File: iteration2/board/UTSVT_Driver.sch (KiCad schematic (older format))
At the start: 4 parts, among them J1 DB37_Female_MountingHoles, U1 Nucleo, U2 SN65HVD230

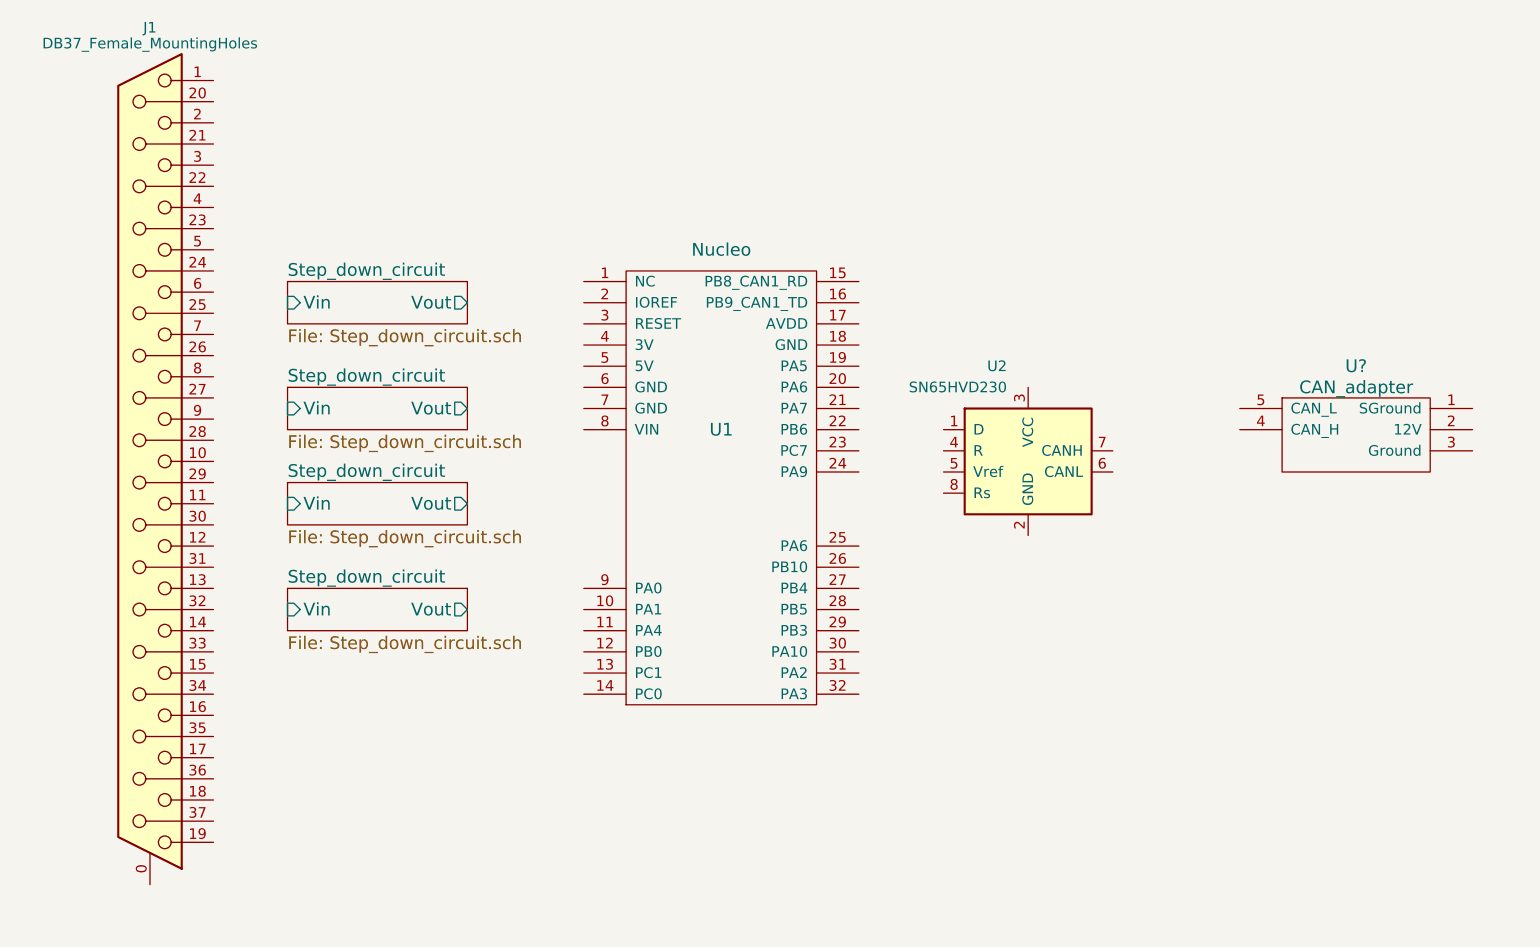
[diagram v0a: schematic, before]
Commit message: Added traces
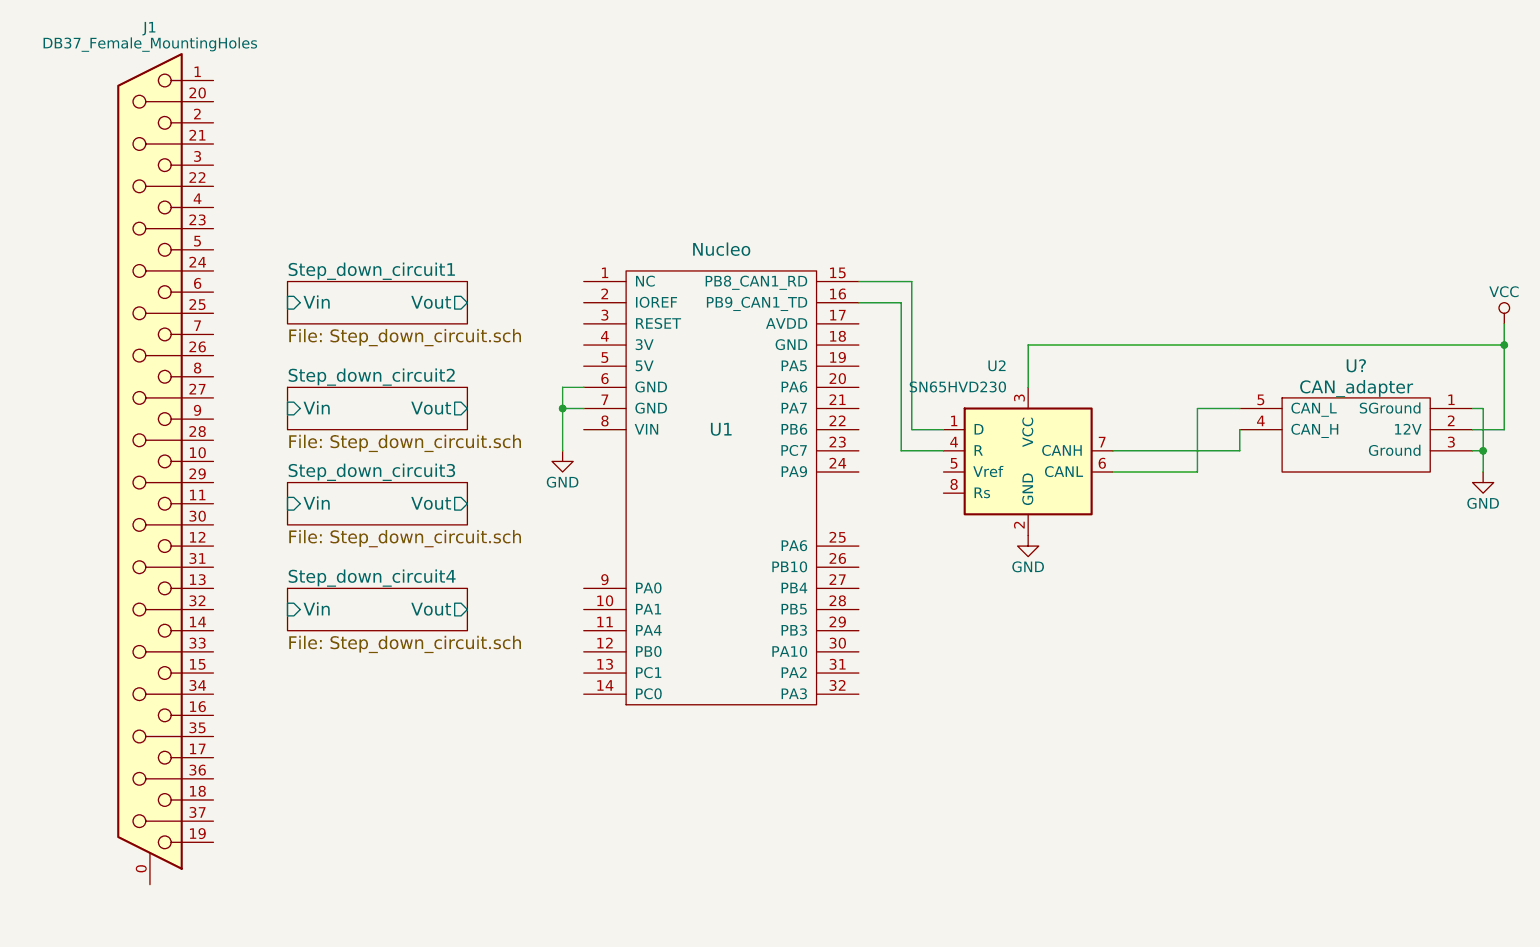
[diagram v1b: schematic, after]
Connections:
- net at U1.15 (PB8_CAN1_RD): now also U2.1 (D)
- net at U1.16 (PB9_CAN1_TD): now also U2.4 (R)
- net GND: now reaches U1.6 (GND)
- net GND: now also U1.7 (GND), U2.2 (GND), U?.1 (SGround), U?.3 (Ground)
- net VCC: now reaches U2.3 (VCC)
- net VCC: now also U?.2 (12V)
- net at U2.6 (CANL): now also U?.5 (CAN_L)
- net at U2.7 (CANH): now also U?.4 (CAN_H)
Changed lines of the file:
@@
 S 4050 3050 850  200
 U 59EC784F
-F0 "Step_down_circuit" 60
+F0 "Step_down_circuit1" 60
 F1 "Step_down_circuit.sch" 60
 F2 "Vin" I L 4050 3150 60
@@
 S 4050 3550 850  200
 U 59EC8586
-F0 "Step_down_circuit" 60
+F0 "Step_down_circuit2" 60
 F1 "Step_down_circuit.sch" 60
 F2 "Vin" I L 4050 3650 60
@@
 S 4050 4000 850  200
 U 59EC8F0E
-F0 "Step_down_circuit" 60
+F0 "Step_down_circuit3" 60
 F1 "Step_down_circuit.sch" 60
 F2 "Vin" I L 4050 4100 60
@@
 S 4050 4500 850  200
 U 59EC8F12
-F0 "Step_down_circuit" 60
+F0 "Step_down_circuit4" 60
 F1 "Step_down_circuit.sch" 60
 F2 "Vin" I L 4050 4600 60
@@
 	1    0    0    -1
 $EndComp
+$Comp
+L GND #PWR?
+U 1 1 59F244D9
+P 9700 3950
+F 0 "#PWR?" H 9700 3700 50  0001 C CNN
+F 1 "GND" H 9700 3800 50  0000 C CNN
+F 2 "" H 9700 3950 50  0001 C CNN
+F 3 "" H 9700 3950 50  0001 C CNN
+	1    9700 3950
+	1    0    0    -1
+$EndComp
+$Comp
+L GND #PWR?
+U 1 1 59F24541
+P 7550 4250
+F 0 "#PWR?" H 7550 4000 50  0001 C CNN
+F 1 "GND" H 7550 4100 50  0000 C CNN
+F 2 "" H 7550 4250 50  0001 C CNN
+F 3 "" H 7550 4250 50  0001 C CNN
+	1    7550 4250
+	1    0    0    -1
+$EndComp
+$Comp
+L GND #PWR?
+U 1 1 59F262C8
+P 5350 3850
+F 0 "#PWR?" H 5350 3600 50  0001 C CNN
+F 1 "GND" H 5350 3700 50  0000 C CNN
+F 2 "" H 5350 3850 50  0001 C CNN
+F 3 "" H 5350 3850 50  0001 C CNN
+	1    5350 3850
+	1    0    0    -1
+$EndComp
+$Comp
+L VCC #PWR?
+U 1 1 59F2677A
+P 9800 3250
+F 0 "#PWR?" H 9800 3100 50  0001 C CNN
+F 1 "VCC" H 9800 3400 50  0000 C CNN
+F 2 "" H 9800 3250 50  0001 C CNN
+F 3 "" H 9800 3250 50  0001 C CNN
+	1    9800 3250
+	1    0    0    -1
+$EndComp
+Wire Wire Line
+	7950 3850 8550 3850
+Wire Wire Line
+	8550 3850 8550 3750
+Wire Wire Line
+	7950 3950 8350 3950
+Wire Wire Line
+	8350 3950 8350 3650
+Wire Wire Line
+	8350 3650 8550 3650
+Wire Wire Line
+	5450 3550 5350 3550
+Wire Wire Line
+	5350 3550 5350 3850
+Wire Wire Line
+	5450 3650 5350 3650
+Connection ~ 5350 3650
+Wire Wire Line
+	6750 3050 7000 3050
+Wire Wire Line
+	7000 3050 7000 3750
+Wire Wire Line
+	7000 3750 7150 3750
+Wire Wire Line
+	6750 3150 6950 3150
+Wire Wire Line
+	6950 3150 6950 3850
+Wire Wire Line
+	6950 3850 7150 3850
+Wire Wire Line
+	9800 3250 9800 3750
+Wire Wire Line
+	9800 3750 9650 3750
+Wire Wire Line
+	9650 3650 9700 3650
+Wire Wire Line
+	9700 3650 9700 3950
+Wire Wire Line
+	9700 3850 9650 3850
+Connection ~ 9700 3850
+Wire Wire Line
+	7550 3550 7550 3350
+Wire Wire Line
+	7550 3350 9800 3350
+Connection ~ 9800 3350
 $EndSCHEMATC

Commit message: Modified to accept potentiometer input
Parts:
- added C?: C, symbol C
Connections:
- net GND: now also C?.1
- net VCC: no longer U2.3 (VCC)
- net step_down_circuit2/Vout: now reaches U1.10 (PA1)
- net step_down_circuit3/Vout: now reaches U1.11 (PA4)
- net step_down_circuit_analog1/Vout: now reaches U1.12 (PB0)
- net step_down_circuit1/Vout: now reaches U1.9 (PA0)
- new net +3V3: C?.2, U2.3 (VCC)
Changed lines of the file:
@@
 S 4050 3050 850  200
 U 59EC784F
-F0 "Step_down_circuit1" 60
-F1 "Step_down_circuit.sch" 60
+F0 "step_down_circuit1" 60
+F1 "step_down_circuit.sch" 60
 F2 "Vin" I L 4050 3150 60
 F3 "Vout" O R 4900 3150 60
@@
 S 4050 3550 850  200
 U 59EC8586
-F0 "Step_down_circuit2" 60
-F1 "Step_down_circuit.sch" 60
+F0 "step_down_circuit2" 60
+F1 "step_down_circuit.sch" 60
 F2 "Vin" I L 4050 3650 60
 F3 "Vout" O R 4900 3650 60
@@
 S 4050 4000 850  200
 U 59EC8F0E
-F0 "Step_down_circuit3" 60
-F1 "Step_down_circuit.sch" 60
+F0 "step_down_circuit3" 60
+F1 "step_down_circuit.sch" 60
 F2 "Vin" I L 4050 4100 60
 F3 "Vout" O R 4900 4100 60
-$EndSheet
-$Sheet
-S 4050 4500 850  200
-U 59EC8F12
-F0 "Step_down_circuit4" 60
-F1 "Step_down_circuit.sch" 60
-F2 "Vin" I L 4050 4600 60
-F3 "Vout" O R 4900 4600 60
 $EndSheet
 $Comp
@@
 	1    0    0    -1
 $EndComp
+$Sheet
+S 4050 4450 850  200
+U 59F275D4
+F0 "step_down_circuit_analog1" 60
+F1 "step_down_circuit_analog.sch" 60
+F2 "Vin" I L 4050 4550 60
+F3 "Vout" O R 4900 4550 60
+$EndSheet
+$Comp
+L GND #PWR?
+U 1 1 59F29663
+P 7850 3350
+F 0 "#PWR?" H 7850 3100 50  0001 C CNN
+F 1 "GND" H 7850 3200 50  0000 C CNN
+F 2 "" H 7850 3350 50  0001 C CNN
+F 3 "" H 7850 3350 50  0001 C CNN
+	1    7850 3350
+	1    0    0    -1
+$EndComp
+$Comp
+L +3.3V #PWR?
+U 1 1 59F296AF
+P 7550 3250
+F 0 "#PWR?" H 7550 3100 50  0001 C CNN
+F 1 "+3.3V" H 7550 3390 50  0000 C CNN
+F 2 "" H 7550 3250 50  0001 C CNN
+F 3 "" H 7550 3250 50  0001 C CNN
+	1    7550 3250
+	1    0    0    -1
+$EndComp
+$Comp
+L C C?
+U 1 1 59F29741
+P 7700 3350
+F 0 "C?" H 7725 3450 50  0000 L CNN
+F 1 "C" H 7725 3250 50  0000 L CNN
+F 2 "" H 7738 3200 50  0001 C CNN
+F 3 "" H 7700 3350 50  0001 C CNN
+	1    7700 3350
+	0    1    1    0
+$EndComp
 Wire Wire Line
 	7950 3850 8550 3850
@@
 	9700 3850 9650 3850
 Connection ~ 9700 3850
+Connection ~ 9800 3350
 Wire Wire Line
-	7550 3550 7550 3350
+	7550 3250 7550 3550
+Connection ~ 7550 3350
 Wire Wire Line
-	7550 3350 9800 3350
-Connection ~ 9800 3350
+	4900 3150 5050 3150
+Wire Wire Line
+	5050 3150 5050 4500
+Wire Wire Line
+	5050 4500 5450 4500
+Wire Wire Line
+	4900 3650 5100 3650
+Wire Wire Line
+	5100 3650 5100 4600
+Wire Wire Line
+	5100 4600 5450 4600
+Wire Wire Line
+	4900 4100 5150 4100
+Wire Wire Line
+	5150 4100 5150 4700
+Wire Wire Line
+	5150 4700 5450 4700
+Wire Wire Line
+	4900 4550 5200 4550
+Wire Wire Line
+	5200 4550 5200 4800
+Wire Wire Line
+	5200 4800 5450 4800
 $EndSCHEMATC

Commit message: Update Netlist
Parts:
- C1: renamed from C?; footprint (none) -> Capacitors_SMD:C_0805_HandSoldering
- U1: footprint (none) -> MotorControllerStuff:AFBShieldBoard
- U3: renamed from U?; footprint (none) -> MotorControllerStuff:CANadapter
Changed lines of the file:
@@
 F 0 "U1" H 6100 4350 60  0000 C CNN
 F 1 "Nucleo" H 6100 5200 60  0000 C CNN
-F 2 "" H 6100 4350 60  0001 C CNN
+F 2 "MotorControllerStuff:AFBShieldBoard" H 6100 4350 60  0001 C CNN
 F 3 "" H 6100 4350 60  0001 C CNN
 	1    6100 4050
@@
 $EndSheet
 $Comp
-L CAN_adapter U?
+L CAN_adapter U3
 U 1 1 59EC9235
 P 9100 3750
-F 0 "U?" H 9100 4050 60  0000 C CNN
+F 0 "U3" H 9100 4050 60  0000 C CNN
 F 1 "CAN_adapter" H 9100 3950 60  0000 C CNN
-F 2 "" H 9150 3750 60  0001 C CNN
+F 2 "MotorControllerStuff:CANadapter" H 9150 3750 60  0001 C CNN
 F 3 "" H 9150 3750 60  0001 C CNN
 	1    9100 3750
@@
 $EndComp
 $Comp
-L GND #PWR?
+L GND #PWR5
 U 1 1 59F244D9
 P 9700 3950
-F 0 "#PWR?" H 9700 3700 50  0001 C CNN
+F 0 "#PWR5" H 9700 3700 50  0001 C CNN
 F 1 "GND" H 9700 3800 50  0000 C CNN
 F 2 "" H 9700 3950 50  0001 C CNN
@@
 $EndComp
 $Comp
-L GND #PWR?
+L GND #PWR3
 U 1 1 59F24541
 P 7550 4250
-F 0 "#PWR?" H 7550 4000 50  0001 C CNN
+F 0 "#PWR3" H 7550 4000 50  0001 C CNN
 F 1 "GND" H 7550 4100 50  0000 C CNN
 F 2 "" H 7550 4250 50  0001 C CNN
@@
 $EndComp
 $Comp
-L GND #PWR?
+L GND #PWR1
 U 1 1 59F262C8
 P 5350 3850
-F 0 "#PWR?" H 5350 3600 50  0001 C CNN
+F 0 "#PWR1" H 5350 3600 50  0001 C CNN
 F 1 "GND" H 5350 3700 50  0000 C CNN
 F 2 "" H 5350 3850 50  0001 C CNN
@@
 $EndComp
 $Comp
-L VCC #PWR?
+L VCC #PWR6
 U 1 1 59F2677A
 P 9800 3250
-F 0 "#PWR?" H 9800 3100 50  0001 C CNN
+F 0 "#PWR6" H 9800 3100 50  0001 C CNN
 F 1 "VCC" H 9800 3400 50  0000 C CNN
 F 2 "" H 9800 3250 50  0001 C CNN
@@
 $EndSheet
 $Comp
-L GND #PWR?
+L GND #PWR4
 U 1 1 59F29663
 P 7850 3350
-F 0 "#PWR?" H 7850 3100 50  0001 C CNN
+F 0 "#PWR4" H 7850 3100 50  0001 C CNN
 F 1 "GND" H 7850 3200 50  0000 C CNN
 F 2 "" H 7850 3350 50  0001 C CNN
@@
 $EndComp
 $Comp
-L +3.3V #PWR?
+L +3.3V #PWR2
 U 1 1 59F296AF
 P 7550 3250
-F 0 "#PWR?" H 7550 3100 50  0001 C CNN
+F 0 "#PWR2" H 7550 3100 50  0001 C CNN
 F 1 "+3.3V" H 7550 3390 50  0000 C CNN
 F 2 "" H 7550 3250 50  0001 C CNN
@@
 $EndComp
 $Comp
-L C C?
+L C C1
 U 1 1 59F29741
 P 7700 3350
-F 0 "C?" H 7725 3450 50  0000 L CNN
+F 0 "C1" H 7725 3450 50  0000 L CNN
 F 1 "C" H 7725 3250 50  0000 L CNN
-F 2 "" H 7738 3200 50  0001 C CNN
+F 2 "Capacitors_SMD:C_0805_HandSoldering" H 7738 3200 50  0001 C CNN
 F 3 "" H 7700 3350 50  0001 C CNN
 	1    7700 3350

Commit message: Redo netlist
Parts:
- J1: footprint (none) -> Connectors_DSub:DB37FC
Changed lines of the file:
@@
 F 0 "J1" H 3400 5950 50  0000 C CNN
 F 1 "DB37_Female_MountingHoles" H 3400 5875 50  0000 C CNN
-F 2 "" H 3400 3900 50  0001 C CNN
+F 2 "Connectors_DSub:DB37FC" H 3400 3900 50  0001 C CNN
 F 3 "" H 3400 3900 50  0001 C CNN
 	1    3400 3900

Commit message: finish wiring
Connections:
- net step_down_circuit1/Vin: now also J1.10
- net step_down_circuit2/Vin: now also J1.12
- net step_down_circuit3/Vin: now also J1.14
- net step_down_circuit_analog1/Vin: now also J1.3
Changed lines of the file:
@@
 $EndComp
 $Comp
-L GND #PWR5
+L GND #PWR01
 U 1 1 59F244D9
 P 9700 3950
-F 0 "#PWR5" H 9700 3700 50  0001 C CNN
+F 0 "#PWR01" H 9700 3700 50  0001 C CNN
 F 1 "GND" H 9700 3800 50  0000 C CNN
 F 2 "" H 9700 3950 50  0001 C CNN
@@
 $EndComp
 $Comp
-L GND #PWR3
+L GND #PWR02
 U 1 1 59F24541
 P 7550 4250
-F 0 "#PWR3" H 7550 4000 50  0001 C CNN
+F 0 "#PWR02" H 7550 4000 50  0001 C CNN
 F 1 "GND" H 7550 4100 50  0000 C CNN
 F 2 "" H 7550 4250 50  0001 C CNN
@@
 $EndComp
 $Comp
-L GND #PWR1
+L GND #PWR03
 U 1 1 59F262C8
 P 5350 3850
-F 0 "#PWR1" H 5350 3600 50  0001 C CNN
+F 0 "#PWR03" H 5350 3600 50  0001 C CNN
 F 1 "GND" H 5350 3700 50  0000 C CNN
 F 2 "" H 5350 3850 50  0001 C CNN
@@
 $EndComp
 $Comp
-L VCC #PWR6
+L VCC #PWR04
 U 1 1 59F2677A
 P 9800 3250
-F 0 "#PWR6" H 9800 3100 50  0001 C CNN
+F 0 "#PWR04" H 9800 3100 50  0001 C CNN
 F 1 "VCC" H 9800 3400 50  0000 C CNN
 F 2 "" H 9800 3250 50  0001 C CNN
@@
 $EndSheet
 $Comp
-L GND #PWR4
+L GND #PWR05
 U 1 1 59F29663
 P 7850 3350
-F 0 "#PWR4" H 7850 3100 50  0001 C CNN
+F 0 "#PWR05" H 7850 3100 50  0001 C CNN
 F 1 "GND" H 7850 3200 50  0000 C CNN
 F 2 "" H 7850 3350 50  0001 C CNN
@@
 $EndComp
 $Comp
-L +3.3V #PWR2
+L +3.3V #PWR06
 U 1 1 59F296AF
 P 7550 3250
-F 0 "#PWR2" H 7550 3100 50  0001 C CNN
+F 0 "#PWR06" H 7550 3100 50  0001 C CNN
 F 1 "+3.3V" H 7550 3390 50  0000 C CNN
 F 2 "" H 7550 3250 50  0001 C CNN
@@
 	5150 4700 5450 4700
 Wire Wire Line
-	4900 4550 5200 4550
+	3700 2500 4000 2500
+Wire Wire Line
+	4000 2500 4000 4550
+Wire Wire Line
+	4000 4550 4050 4550
+Wire Wire Line
+	3700 4300 3950 4300
+Wire Wire Line
+	3950 4300 3950 3650
+Wire Wire Line
+	3950 3650 4050 3650
+Wire Wire Line
+	3700 3900 3900 3900
+Wire Wire Line
+	3900 3900 3900 3150
+Wire Wire Line
+	3900 3150 4050 3150
+Wire Wire Line
+	3700 4700 3900 4700
+Wire Wire Line
+	3900 4700 3900 4100
+Wire Wire Line
+	3900 4100 4050 4100
 Wire Wire Line
 	5200 4550 5200 4800
 Wire Wire Line
 	5200 4800 5450 4800
+Wire Wire Line
+	4900 4550 5200 4550
 $EndSCHEMATC

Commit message: Generated netlist
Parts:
- U1: footprint MotorControllerStuff:AFBShieldBoard -> UTSVT_board:AFBShieldBoard
- U3: footprint MotorControllerStuff:CANadapter -> UTSVT_board:CAN_adapter
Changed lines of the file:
@@
 F 0 "U1" H 6100 4350 60  0000 C CNN
 F 1 "Nucleo" H 6100 5200 60  0000 C CNN
-F 2 "MotorControllerStuff:AFBShieldBoard" H 6100 4350 60  0001 C CNN
+F 2 "UTSVT_board:AFBShieldBoard" H 6100 4350 60  0001 C CNN
 F 3 "" H 6100 4350 60  0001 C CNN
 	1    6100 4050
@@
 F 0 "U3" H 9100 4050 60  0000 C CNN
 F 1 "CAN_adapter" H 9100 3950 60  0000 C CNN
-F 2 "MotorControllerStuff:CANadapter" H 9150 3750 60  0001 C CNN
+F 2 "UTSVT_board:CAN_adapter" H 9150 3750 60  0001 C CNN
 F 3 "" H 9150 3750 60  0001 C CNN
 	1    9100 3750

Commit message: Redid some components to fit footprint
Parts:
- J1: footprint Connectors_DSub:DB37FC -> UTSVT_board:DB37FC
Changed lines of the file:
@@
 $EndDescr
-$Comp
-L Nucleo U1
-U 1 1 59EB7F2F
-P 6100 4050
-F 0 "U1" H 6100 4350 60  0000 C CNN
-F 1 "Nucleo" H 6100 5200 60  0000 C CNN
-F 2 "UTSVT_board:AFBShieldBoard" H 6100 4350 60  0001 C CNN
-F 3 "" H 6100 4350 60  0001 C CNN
-	1    6100 4050
-	1    0    0    -1
-$EndComp
 $Comp
 L DB37_Female_MountingHoles J1
@@
 F 0 "J1" H 3400 5950 50  0000 C CNN
 F 1 "DB37_Female_MountingHoles" H 3400 5875 50  0000 C CNN
-F 2 "Connectors_DSub:DB37FC" H 3400 3900 50  0001 C CNN
+F 2 "UTSVT_board:DB37FC" H 3400 3900 50  0001 C CNN
 F 3 "" H 3400 3900 50  0001 C CNN
 	1    3400 3900
@@
 Wire Wire Line
 	4900 4550 5200 4550
+$Comp
+L Nucleo U1
+U 1 1 59F29930
+P 6100 4050
+F 0 "U1" H 6100 4350 60  0000 C CNN
+F 1 "Nucleo" H 6100 5200 60  0000 C CNN
+F 2 "UTSVT_board:AFBShieldBoard" H 6100 4350 60  0001 C CNN
+F 3 "" H 6100 4350 60  0001 C CNN
+	1    6100 4050
+	1    0    0    -1
+$EndComp
 $EndSCHEMATC
